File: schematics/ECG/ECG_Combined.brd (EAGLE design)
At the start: 25.4 x 25.4 mm, 66 parts, among them IC1 ADS1293, IC2 LIS3DH, IC3 MCP1703, IC4 CC2541, IC5 FSA4157, IC6 FSA4157, IC7 FSA4157, X1 XTAL-2SMD, X2 XTAL_403, X3 XTAL-CSM7

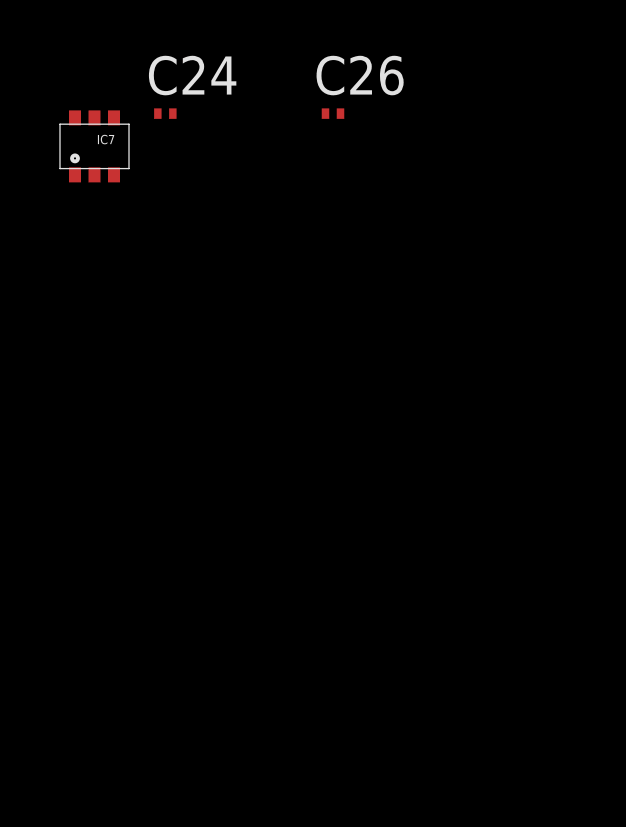
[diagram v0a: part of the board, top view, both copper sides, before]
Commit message: added analog switch for ads1293 power. added jumper for ads1293 xtal gnd/vcc connection
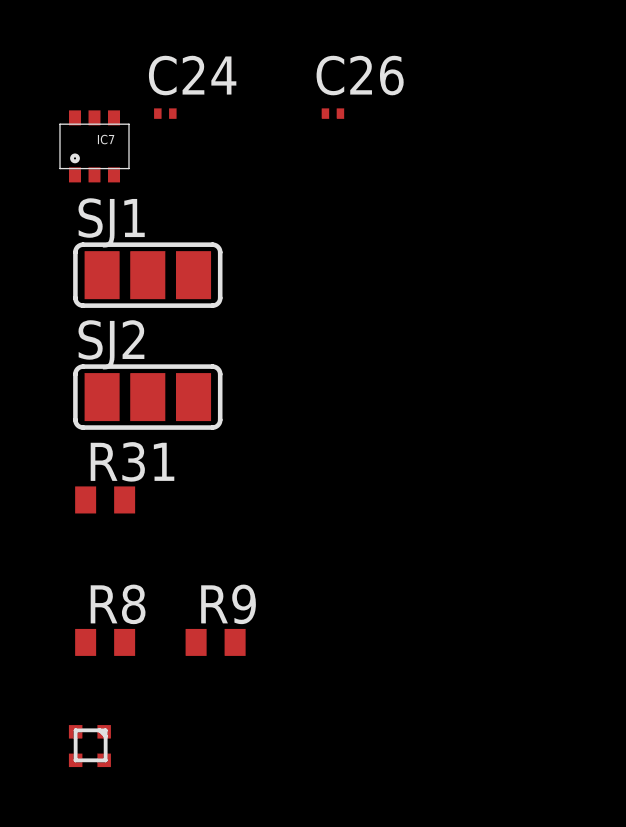
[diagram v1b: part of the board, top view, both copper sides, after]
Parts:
- added R31, R8, R9: 1K, rcl:R0402
- added SJ1, SJ2: (no value), jumper:SJ_2
- added TRI_LED: SML-LX0404SIUPGUSB, lumex:SML-LX0404SIUPGUSB
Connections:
- new net BLUE_LED: IC4.36, R31.2
- new net ECG_VCC: IC1.22, IC1.28, IC7.4
- new net ECG_VCC_SW: IC4.5, IC7.6
- new net GREEN_LED: IC4.38, R8.2
- new net N$10: C2.2, SJ1.2
- new net N$13: C1.2, SJ2.2
- new net N$20: R8.1, TRI_LED.2
- new net N$3: R9.1, TRI_LED.3
- new net N$9: R31.1, TRI_LED.4
- new net RED_LED: IC4.37, R9.2
- net GND: now also IC7.2, IC7.3, SJ1.3, SJ2.3
- net VCC: now also IC7.1, IC7.5, SJ1.1, SJ2.1, TRI_LED.1; no longer C1.1, C2.1, IC1.22, IC1.28
- net XTAL1: now also C1.1, X3.1; no longer C2.2, X3.2
- net XTAL2: now also C2.1, X3.2; no longer C1.2, X3.1
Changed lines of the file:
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@@
 <layer number="110" name="fp0" color="7" fill="1" visible="no" active="yes"/>
 <layer number="111" name="LPC17xx" color="7" fill="1" visible="yes" active="yes"/>
+<layer number="112" name="tSilk" color="7" fill="1" visible="yes" active="yes"/>
 <layer number="116" name="Patch_BOT" color="9" fill="4" visible="yes" active="yes"/>
 <layer number="121" name="_tsilk" color="7" fill="1" visible="yes" active="yes"/>
@@
 <layer number="124" name="bTestmark" color="7" fill="1" visible="no" active="yes"/>
 <layer number="125" name="_tNames" color="7" fill="1" visible="yes" active="yes"/>
+<layer number="126" name="_bNames" color="7" fill="1" visible="yes" active="yes"/>
+<layer number="127" name="_tValues" color="7" fill="1" visible="yes" active="yes"/>
+<layer number="128" name="_bValues" color="7" fill="1" visible="yes" active="yes"/>
 <layer number="131" name="tAdjust" color="7" fill="1" visible="no" active="yes"/>
 <layer number="132" name="bAdjust" color="7" fill="1" visible="no" active="yes"/>
 <layer number="144" name="Drill_legend" color="7" fill="1" visible="yes" active="yes"/>
 <layer number="151" name="HeatSink" color="7" fill="1" visible="yes" active="yes"/>
+<layer number="152" name="_bDocu" color="7" fill="1" visible="yes" active="yes"/>
 <layer number="199" name="Contour" color="7" fill="1" visible="yes" active="yes"/>
 <layer number="200" name="200bmp" color="1" fill="10" visible="no" active="no"/>
@@
 <layer number="232" name="Eagle3D_PG2" color="14" fill="2" visible="yes" active="yes"/>
 <layer number="233" name="Eagle3D_PG3" color="14" fill="4" visible="yes" active="yes"/>
+<layer number="248" name="Housing" color="7" fill="1" visible="yes" active="yes"/>
+<layer number="249" name="Edge" color="7" fill="1" visible="yes" active="yes"/>
 <layer number="250" name="Descript" color="3" fill="1" visible="no" active="no"/>
 <layer number="251" name="SMDround" color="12" fill="11" visible="no" active="no"/>
@@
 <element name="C26" library="rcl" package="C0201" value="1.0uF" x="-51.2826" y="-58.5978"/>
 <element name="IC7" library="fairchild" package="SC70-6" value="FSA4157" x="-59.182" y="-59.69"/>
+<element name="SJ1" library="jumper" package="SJ_2" value="" x="-57.4548" y="-63.9826"/>
+<element name="SJ2" library="jumper" package="SJ_2" value="" x="-57.4548" y="-68.0466"/>
+<element name="R8" library="rcl" package="R0402" value="1K" x="-58.8772" y="-76.2254"/>
+<element name="R31" library="rcl" package="R0402" value="1K" x="-58.8772" y="-71.4756"/>
+<element name="TRI_LED" library="lumex" package="SML-LX0404SIUPGUSB" value="SML-LX0404SIUPGUSB" x="-59.3598" y="-79.6544"/>
+<element name="R9" library="rcl" package="R0402" value="1K" x="-55.1942" y="-76.2254"/>
 </elements>
 <signals>
@@
 <contactref element="C24" pad="2"/>
 <contactref element="C26" pad="2"/>
+<contactref element="SJ2" pad="3"/>
+<contactref element="SJ1" pad="3"/>
+<contactref element="IC7" pad="3"/>
+<contactref element="IC7" pad="2"/>
+<wire x1="-55.9308" y1="-63.9826" x2="-55.9308" y2="-68.0466" width="0" layer="19" extent="1-1"/>
+<wire x1="-58.582" y1="-60.64" x2="-55.9308" y2="-63.9826" width="0" layer="19" extent="1-1"/>
+<wire x1="-59.232" y1="-60.64" x2="-58.582" y2="-60.64" width="0" layer="19" extent="1-1"/>
+<wire x1="-56.6206" y1="-58.5978" x2="-58.582" y2="-60.64" width="0" layer="19" extent="1-1"/>
 <wire x1="-56.6206" y1="-53.848" x2="-56.6206" y2="-58.5978" width="0" layer="19" extent="1-1"/>
 <wire x1="-56.6206" y1="-49.0982" x2="-56.6206" y2="-53.848" width="0" layer="19" extent="1-1"/>
@@
 <contactref element="IC4" pad="10"/>
 <contactref element="IC4" pad="39"/>
-<contactref element="IC1" pad="22"/>
 <contactref element="C7" pad="1"/>
 <contactref element="C8" pad="1"/>
-<contactref element="IC1" pad="28"/>
-<contactref element="C2" pad="1"/>
-<contactref element="C1" pad="1"/>
 <contactref element="CONN1" pad="2"/>
 <contactref element="IC3" pad="2"/>
@@
 <contactref element="C24" pad="1"/>
 <contactref element="C26" pad="1"/>
+<contactref element="SJ2" pad="1"/>
+<contactref element="SJ1" pad="1"/>
+<contactref element="IC7" pad="1"/>
+<contactref element="IC7" pad="5"/>
+<contactref element="TRI_LED" pad="1"/>
+<wire x1="-58.9788" y1="-68.0466" x2="-58.9098" y2="-79.2044" width="0" layer="19" extent="1-1"/>
+<wire x1="-58.9788" y1="-63.9826" x2="-58.9788" y2="-68.0466" width="0" layer="19" extent="1-1"/>
+<wire x1="-59.882" y1="-60.64" x2="-58.9788" y2="-63.9826" width="0" layer="19" extent="1-1"/>
+<wire x1="-59.232" y1="-58.74" x2="-59.882" y2="-60.64" width="0" layer="19" extent="1-1"/>
+<wire x1="-57.1206" y1="-58.5978" x2="-59.232" y2="-58.74" width="0" layer="19" extent="1-1"/>
 <wire x1="-57.1206" y1="-53.848" x2="-57.1206" y2="-58.5978" width="0" layer="19" extent="1-1"/>
 <wire x1="-57.1206" y1="-49.0982" x2="-57.1206" y2="-53.848" width="0" layer="19" extent="1-1"/>
@@
 <wire x1="2.7392" y1="6.604" x2="2.6214" y2="3.2152" width="0" layer="19" extent="1-1"/>
 <wire x1="3.4304" y1="6.6208" x2="2.7392" y2="6.604" width="0" layer="19" extent="1-1"/>
-<wire x1="7.4168" y1="4.6188" x2="3.4304" y2="6.6208" width="0" layer="19" extent="1-1"/>
 <wire x1="6.785" y1="9.9918" x2="3.4304" y2="6.6208" width="0" layer="19" extent="1-1"/>
 <wire x1="7.435" y1="11.8918" x2="6.785" y2="9.9918" width="0" layer="19" extent="1-1"/>
@@
 <wire x1="15.9276" y1="16.3242" x2="15.9276" y2="17.8242" width="0" layer="19" extent="1-1"/>
 <wire x1="1.8954" y1="18.1308" x2="9.9276" y2="16.3242" width="0" layer="19" extent="1-1"/>
-<wire x1="15.6538" y1="6.203" x2="7.4168" y2="4.6188" width="0" layer="19" extent="1-1"/>
-<wire x1="18.6538" y1="6.203" x2="15.6538" y2="6.203" width="0" layer="19" extent="1-1"/>
-<wire x1="19.7104" y1="4.6188" x2="18.6538" y2="6.203" width="0" layer="19" extent="1-1"/>
 <wire x1="-24.38" y1="34.29" x2="1.8954" y2="18.1308" width="0" layer="19" extent="1-1"/>
 <wire x1="-30.73" y1="34.29" x2="-24.38" y2="34.29" width="0" layer="19" extent="1-1"/>
@@
 <signal name="XTAL2">
 <contactref element="IC1" pad="24"/>
-<contactref element="X3" pad="1"/>
-<contactref element="C1" pad="2"/>
-<wire x1="19.7104" y1="4.1188" x2="16.6538" y2="6.203" width="0" layer="19" extent="1-1"/>
-<wire x1="18.3186" y1="2.664" x2="19.7104" y2="4.1188" width="0" layer="19" extent="1-1"/>
+<contactref element="X3" pad="2"/>
+<contactref element="C2" pad="1"/>
+<wire x1="8.9186" y1="2.664" x2="16.6538" y2="6.203" width="0" layer="19" extent="1-1"/>
+<wire x1="7.4168" y1="4.6188" x2="8.9186" y2="2.664" width="0" layer="19" extent="1-1"/>
 </signal>
 <signal name="XTAL1">
 <contactref element="IC1" pad="23"/>
-<contactref element="X3" pad="2"/>
-<contactref element="C2" pad="2"/>
-<wire x1="8.9186" y1="2.664" x2="16.1538" y2="6.203" width="0" layer="19" extent="1-1"/>
-<wire x1="7.4168" y1="4.1188" x2="8.9186" y2="2.664" width="0" layer="19" extent="1-1"/>
+<contactref element="X3" pad="1"/>
+<contactref element="C1" pad="1"/>
+<wire x1="19.7104" y1="4.6188" x2="16.1538" y2="6.203" width="0" layer="19" extent="1-1"/>
+<wire x1="18.3186" y1="2.664" x2="19.7104" y2="4.6188" width="0" layer="19" extent="1-1"/>
 </signal>
 <signal name="IN3">
@@
 <wire x1="14.7538" y1="7.103" x2="-57" y2="-41" width="0" layer="19" extent="1-1"/>
 </signal>
+<signal name="N$10">
+<contactref element="SJ1" pad="2"/>
+<contactref element="C2" pad="2"/>
+<wire x1="7.4168" y1="4.1188" x2="-57.4548" y2="-63.9826" width="0" layer="19" extent="1-1"/>
+</signal>
+<signal name="N$13">
+<contactref element="SJ2" pad="2"/>
+<contactref element="C1" pad="2"/>
+<wire x1="19.7104" y1="4.1188" x2="-57.4548" y2="-68.0466" width="0" layer="19" extent="1-1"/>
+</signal>
+<signal name="ECG_VCC_SW">
+<contactref element="IC7" pad="6"/>
+<contactref element="IC4" pad="5"/>
+<wire x1="9.9276" y1="18.8242" x2="-59.882" y2="-58.74" width="0" layer="19" extent="1-1"/>
+</signal>
+<signal name="ECG_VCC">
+<contactref element="IC7" pad="4"/>
+<contactref element="IC1" pad="28"/>
+<contactref element="IC1" pad="22"/>
+<wire x1="15.6538" y1="6.203" x2="-58.582" y2="-58.74" width="0" layer="19" extent="1-1"/>
+<wire x1="18.6538" y1="6.203" x2="15.6538" y2="6.203" width="0" layer="19" extent="1-1"/>
+</signal>
+<signal name="BLUE_LED">
+<contactref element="R31" pad="2"/>
+<contactref element="IC4" pad="36"/>
+<wire x1="12.6776" y1="21.5742" x2="-58.2272" y2="-71.4756" width="0" layer="19" extent="1-1"/>
+</signal>
+<signal name="GREEN_LED">
+<contactref element="R8" pad="2"/>
+<contactref element="IC4" pad="38"/>
+<wire x1="11.6776" y1="21.5742" x2="-58.2272" y2="-76.2254" width="0" layer="19" extent="1-1"/>
+</signal>
+<signal name="N$3">
+<contactref element="TRI_LED" pad="3"/>
+<contactref element="R9" pad="1"/>
+<wire x1="-55.8442" y1="-76.2254" x2="-59.8598" y2="-80.1544" width="0" layer="19" extent="1-1"/>
+</signal>
+<signal name="N$9">
+<contactref element="TRI_LED" pad="4"/>
+<contactref element="R31" pad="1"/>
+<wire x1="-59.5272" y1="-71.4756" x2="-59.8598" y2="-79.2044" width="0" layer="19" extent="1-1"/>
+</signal>
+<signal name="N$20">
+<contactref element="TRI_LED" pad="2"/>
+<contactref element="R8" pad="1"/>
+<wire x1="-59.5272" y1="-76.2254" x2="-58.9098" y2="-80.1544" width="0" layer="19" extent="1-1"/>
+</signal>
+<signal name="RED_LED">
+<contactref element="R9" pad="2"/>
+<contactref element="IC4" pad="37"/>
+<wire x1="12.1776" y1="21.5742" x2="-54.5442" y2="-76.2254" width="0" layer="19" extent="1-1"/>
+</signal>
 </signals>
